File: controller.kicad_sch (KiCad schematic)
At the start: 33 parts, among them J10 Header_07x01_2.54mm_0mm_Strai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, J4 Header_03x01_2.54mm_0mm_Strai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, J6 Header_03x01_2.54mm_0mm_Strai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, J9 Header_07x01_2.54mm_0mm_Strai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, U4 STM32H742VGT6

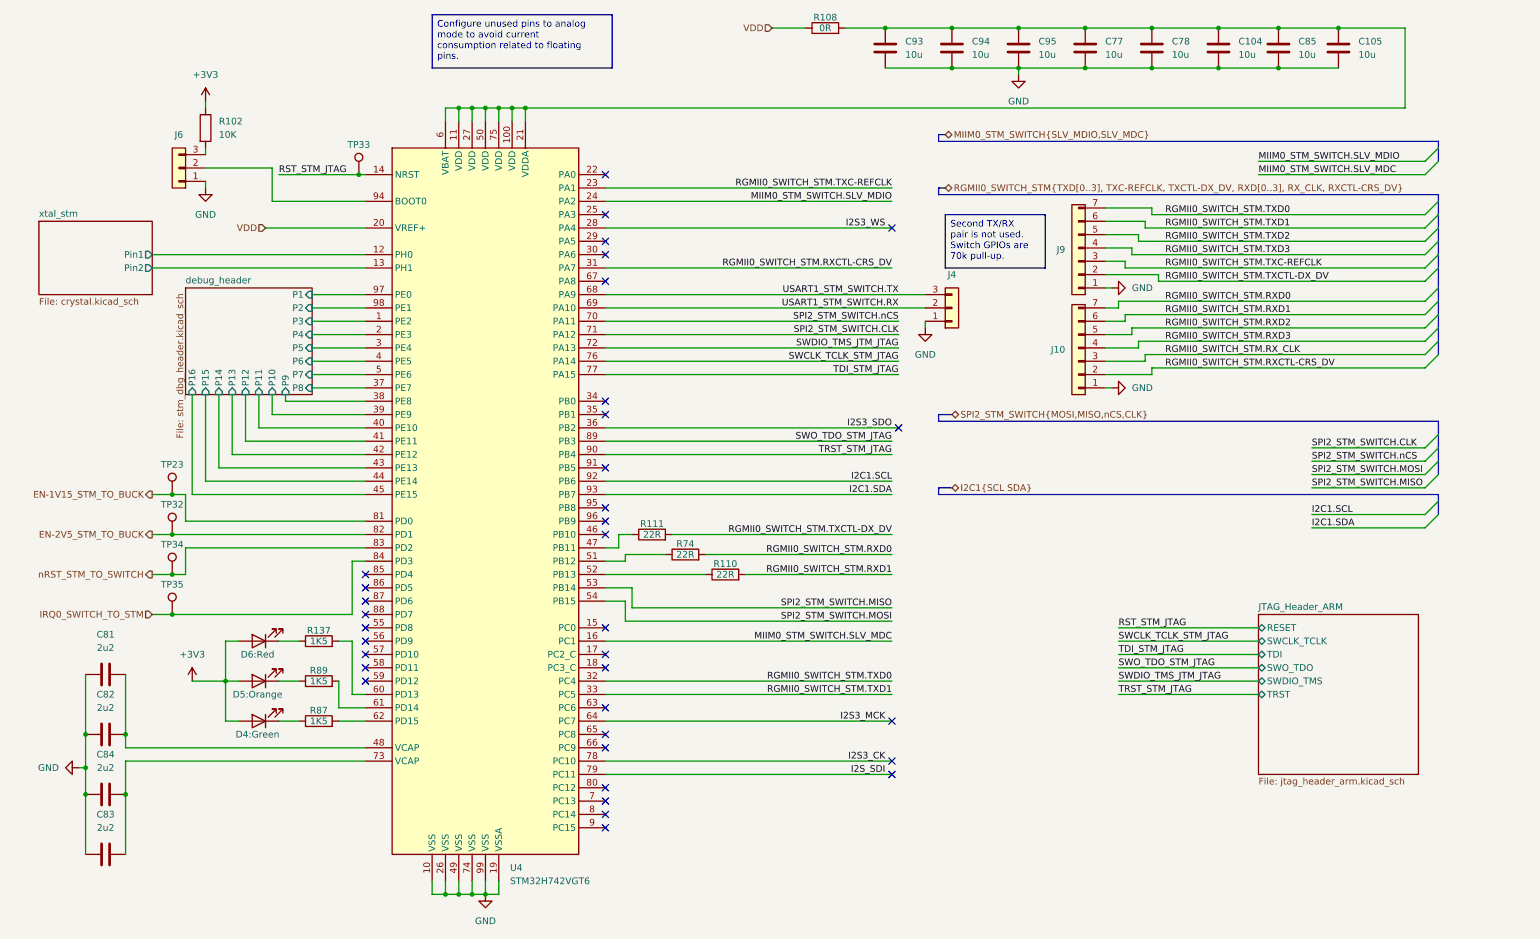
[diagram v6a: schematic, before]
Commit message: moves all STM32 power behind the 0R resistor. Refs: #57
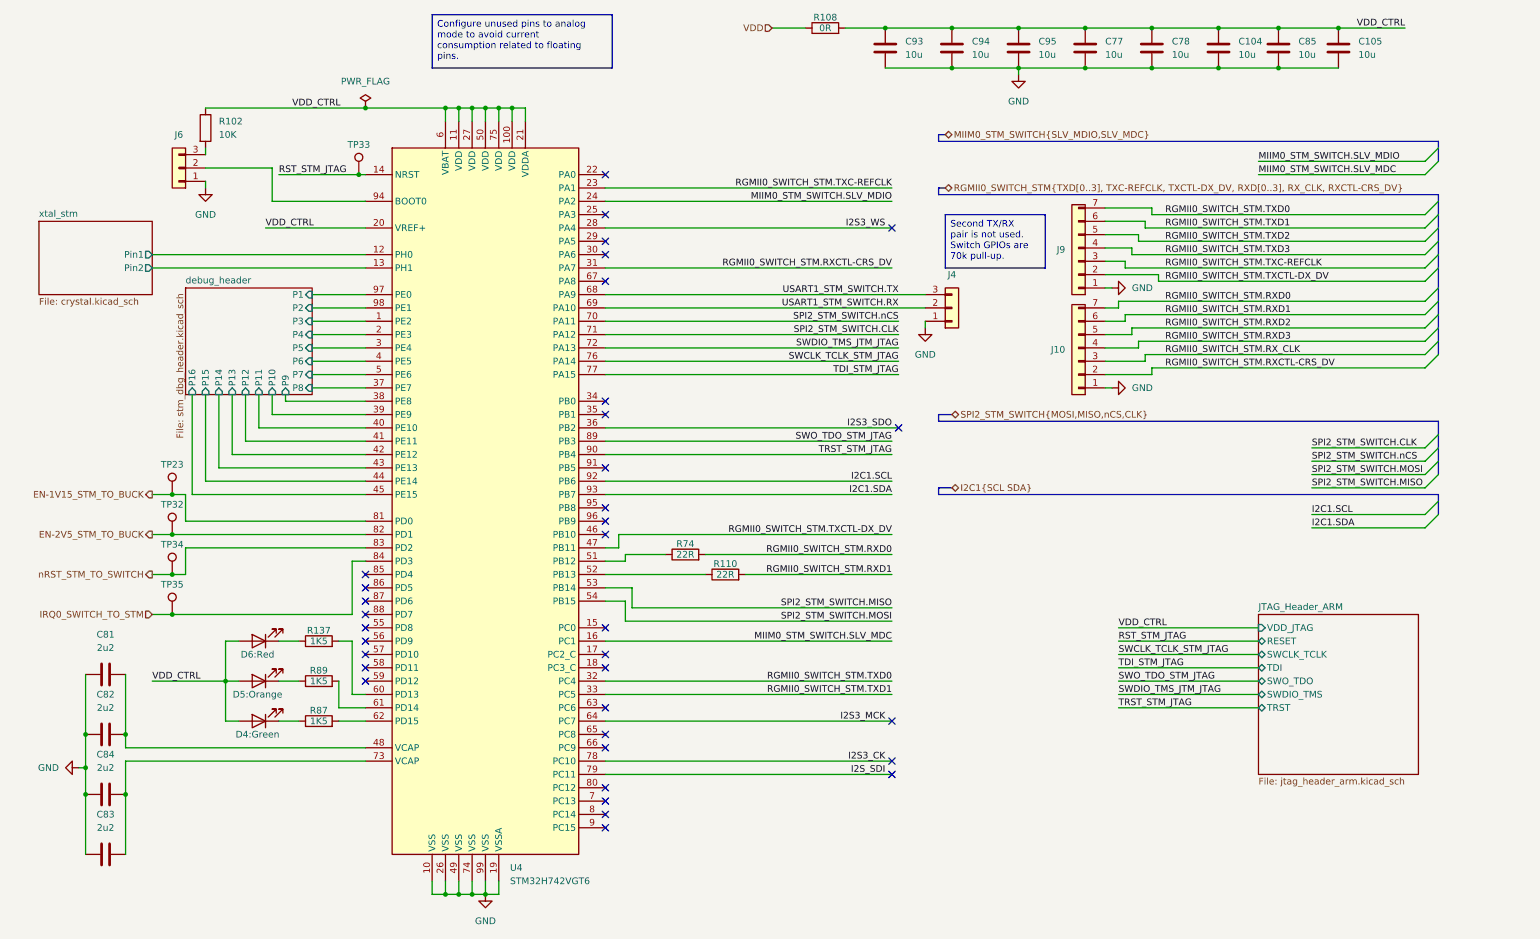
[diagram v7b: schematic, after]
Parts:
- removed R111: 22R, KL_Footprints:R_0603, symbol KL_R:R_22R_0.1W_1pct_0603
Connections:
- net +3V3 is gone; now on net VDD_CTRL: D4.2 (A), D5.2 (A), D6.2 (A), R102.1
- net RGMII0_SWITCH_STM.TXCTL-DX_DV: now also U4.47 (PB11)
- net VDD: no longer U4.20 (VREF+)
- net VDD_CTRL: now reaches C104.1, C105.1, C77.1, C78.1, C85.1, C93.1, C94.1, C95.1, R108.2, U4.100 (VDD), U4.11 (VDD), U4.21 (VDDA), U4.27 (VDD), U4.50 (VDD), U4.6 (VBAT), U4.75 (VDD)
- net VDD_CTRL: now also U4.20 (VREF+)
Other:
- sheet JTAG_Header_ARM ports: added VDD_JTAG; removed none

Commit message: layout v1
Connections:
- net RGMII0_SWITCH_STM.TXC-REFCLK: now also J9.7 (Pin_3); no longer J9.3 (Pin_3)
- net RGMII0_SWITCH_STM.TXCTL-DX_DV: now also J9.6 (Pin_3); no longer J9.2 (Pin_2)
- net RGMII0_SWITCH_STM.TXD0: now also J9.5 (Pin_2); no longer J9.7 (Pin_3)
- net RGMII0_SWITCH_STM.TXD1: now also J9.4 (Pin_1); no longer J9.6 (Pin_3)
- net RGMII0_SWITCH_STM.TXD2: now also J9.3 (Pin_3); no longer J9.5 (Pin_2)
- net RGMII0_SWITCH_STM.TXD3: now also J9.2 (Pin_2); no longer J9.4 (Pin_1)
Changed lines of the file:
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@@
 	)
 	(label "RGMII0_SWITCH_STM.TXCTL-DX_DV"
-		(at 231.14 64.77 0)
+		(at 231.14 54.61 0)
 		(effects
 			(font
@@
 	)
 	(label "RGMII0_SWITCH_STM.TXD3"
-		(at 231.14 59.69 0)
+		(at 231.14 64.77 0)
 		(effects
 			(font
@@
 	)
 	(label "RGMII0_SWITCH_STM.TXC-REFCLK"
-		(at 231.14 62.23 0)
+		(at 231.14 52.07 0)
 		(effects
 			(font
@@
 	)
 	(label "RGMII0_SWITCH_STM.TXD2"
-		(at 231.14 57.15 0)
+		(at 231.14 62.23 0)
 		(effects
 			(font
@@
 	)
 	(label "RGMII0_SWITCH_STM.TXD1"
-		(at 231.14 54.61 0)
+		(at 231.14 59.69 0)
 		(effects
 			(font
@@
 	)
 	(label "RGMII0_SWITCH_STM.TXD0"
-		(at 231.14 52.07 0)
+		(at 231.14 57.15 0)
 		(effects
 			(font
@@
 		)
 	)
+	(netclass_flag ""
+		(length 1.27)
+		(shape round)
+		(at 129.5404 116.84 0)
+		(fields_autoplaced yes)
+		(effects
+			(font
+				(size 1.27 1.27)
+			)
+			(justify left bottom)
+		)
+		(property "Net Class" "RGMII"
+			(at 130.2389 115.57 0)
+			(show_name no)
+			(do_not_autoplace no)
+			(effects
+				(font
+					(size 1.27 1.27)
+				)
+				(justify left)
+			)
+		)
+		(property "Component Class" ""
+			(at -64.7696 67.31 0)
+			(show_name no)
+			(do_not_autoplace no)
+			(effects
+				(font
+					(size 1.27 1.27)
+					(italic yes)
+				)
+			)
+		)
+	)
+	(netclass_flag ""
+		(length 1.27)
+		(shape round)
+		(at 129.54 120.65 0)
+		(fields_autoplaced yes)
+		(effects
+			(font
+				(size 1.27 1.27)
+			)
+			(justify left bottom)
+		)
+		(property "Net Class" "RGMII"
+			(at 130.2385 119.38 0)
+			(show_name no)
+			(do_not_autoplace no)
+			(effects
+				(font
+					(size 1.27 1.27)
+				)
+				(justify left)
+			)
+		)
+		(property "Component Class" ""
+			(at -64.77 71.12 0)
+			(show_name no)
+			(do_not_autoplace no)
+			(effects
+				(font
+					(size 1.27 1.27)
+					(italic yes)
+				)
+			)
+		)
+	)
